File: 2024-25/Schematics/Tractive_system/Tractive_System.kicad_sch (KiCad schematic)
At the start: 20 parts, among them J1 Conn_01x03_Pin, J13 Conn_01x03_Pin, J14 BU-P72930-0, J15 UPCR012ALS2, J16 UPCR012ALS1, J17 EM30MSD-A(06), J18 1-66103-8, J19 1-66399-0, J3 Molex 33472-4001, J4 UPCR012ALS2, J5 Conn_01x02_Pin, J6 UPCR012ALS1, J7 Conn_01x02_Socket

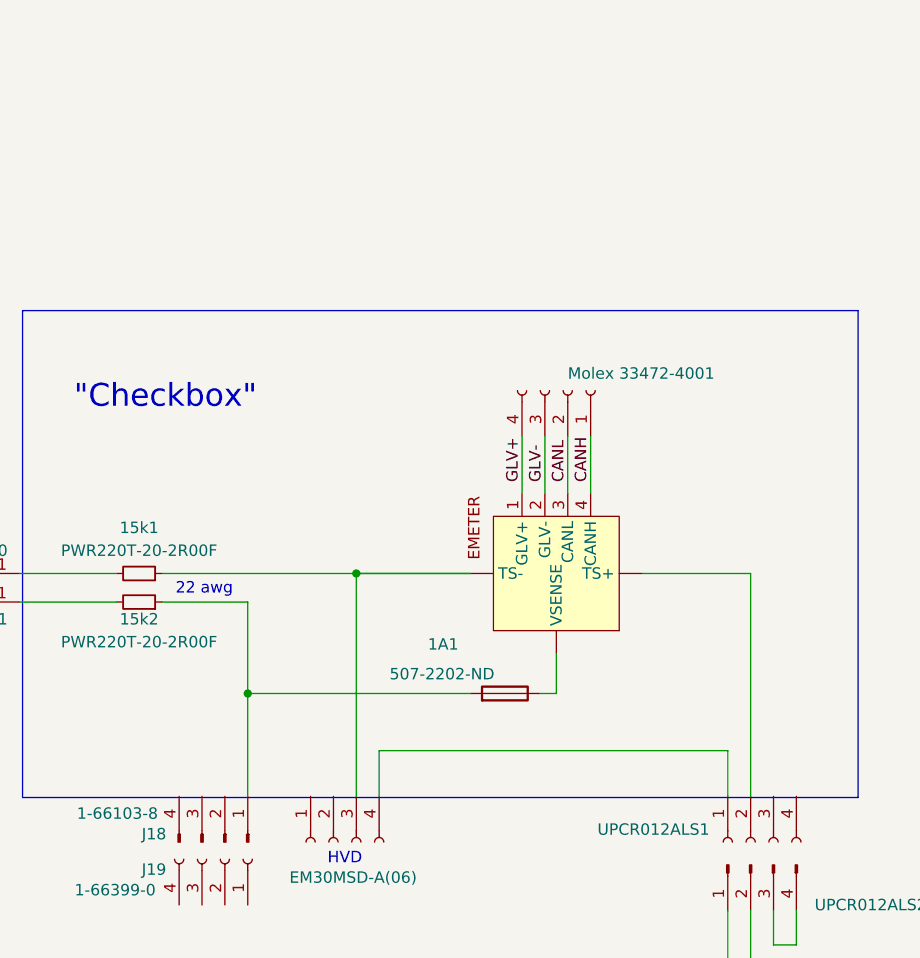
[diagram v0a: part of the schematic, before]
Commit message: Updated tractive system schematic to new energy meter
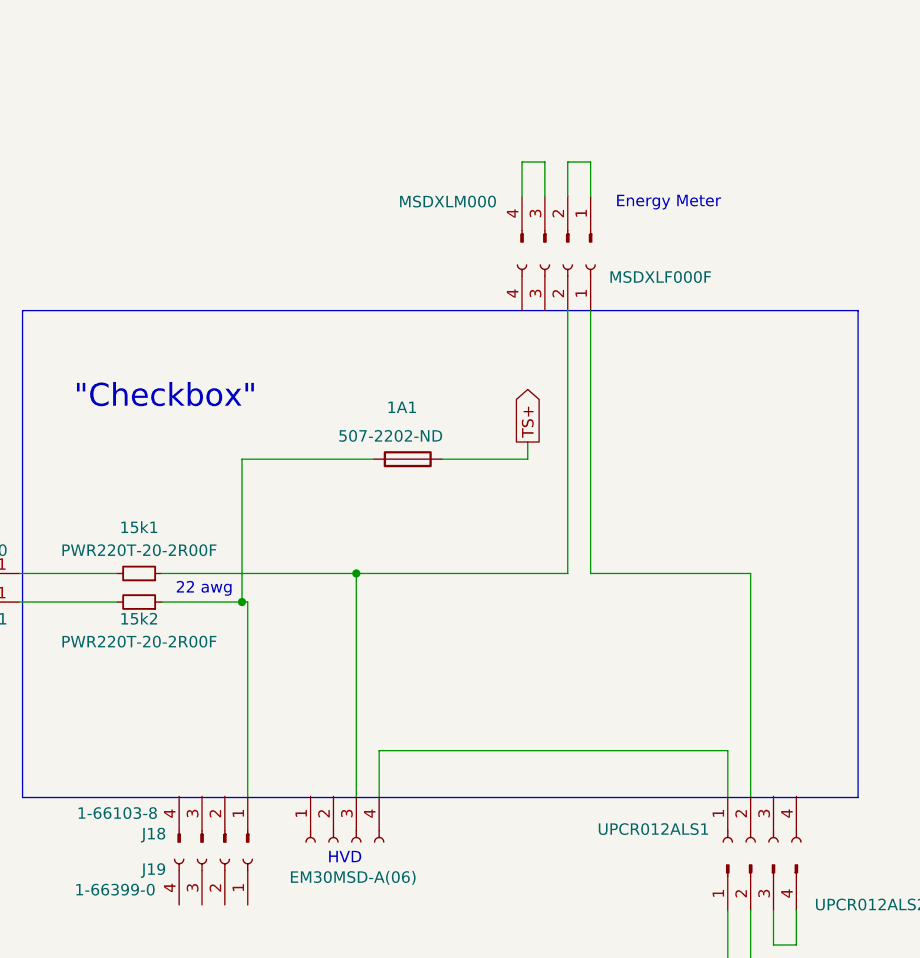
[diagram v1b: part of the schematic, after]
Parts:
- removed J3: Molex 33472-4001, symbol Connector:Conn_01x04_Socket
- removed U1: ~, symbol FSAE:Emeter
- added J8: MSDXLF000F, symbol Connector:Conn_01x04_Socket
- added J9: MSDXLM000, symbol Connector:Conn_01x04_Pin
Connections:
- net at 15k1.1, J17.3 (Pin_3): now also J8.2 (Pin_2)
- net at J16.2 (Pin_2): now also J8.1 (Pin_1)
- net TS+: now reaches 1A1.1
- new net: J9.1 (Pin_1), J9.2 (Pin_2)
- new net: J9.3 (Pin_3), J9.4 (Pin_4)
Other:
- note added: "Energy Meter"
- moved on the sheet: 1A1

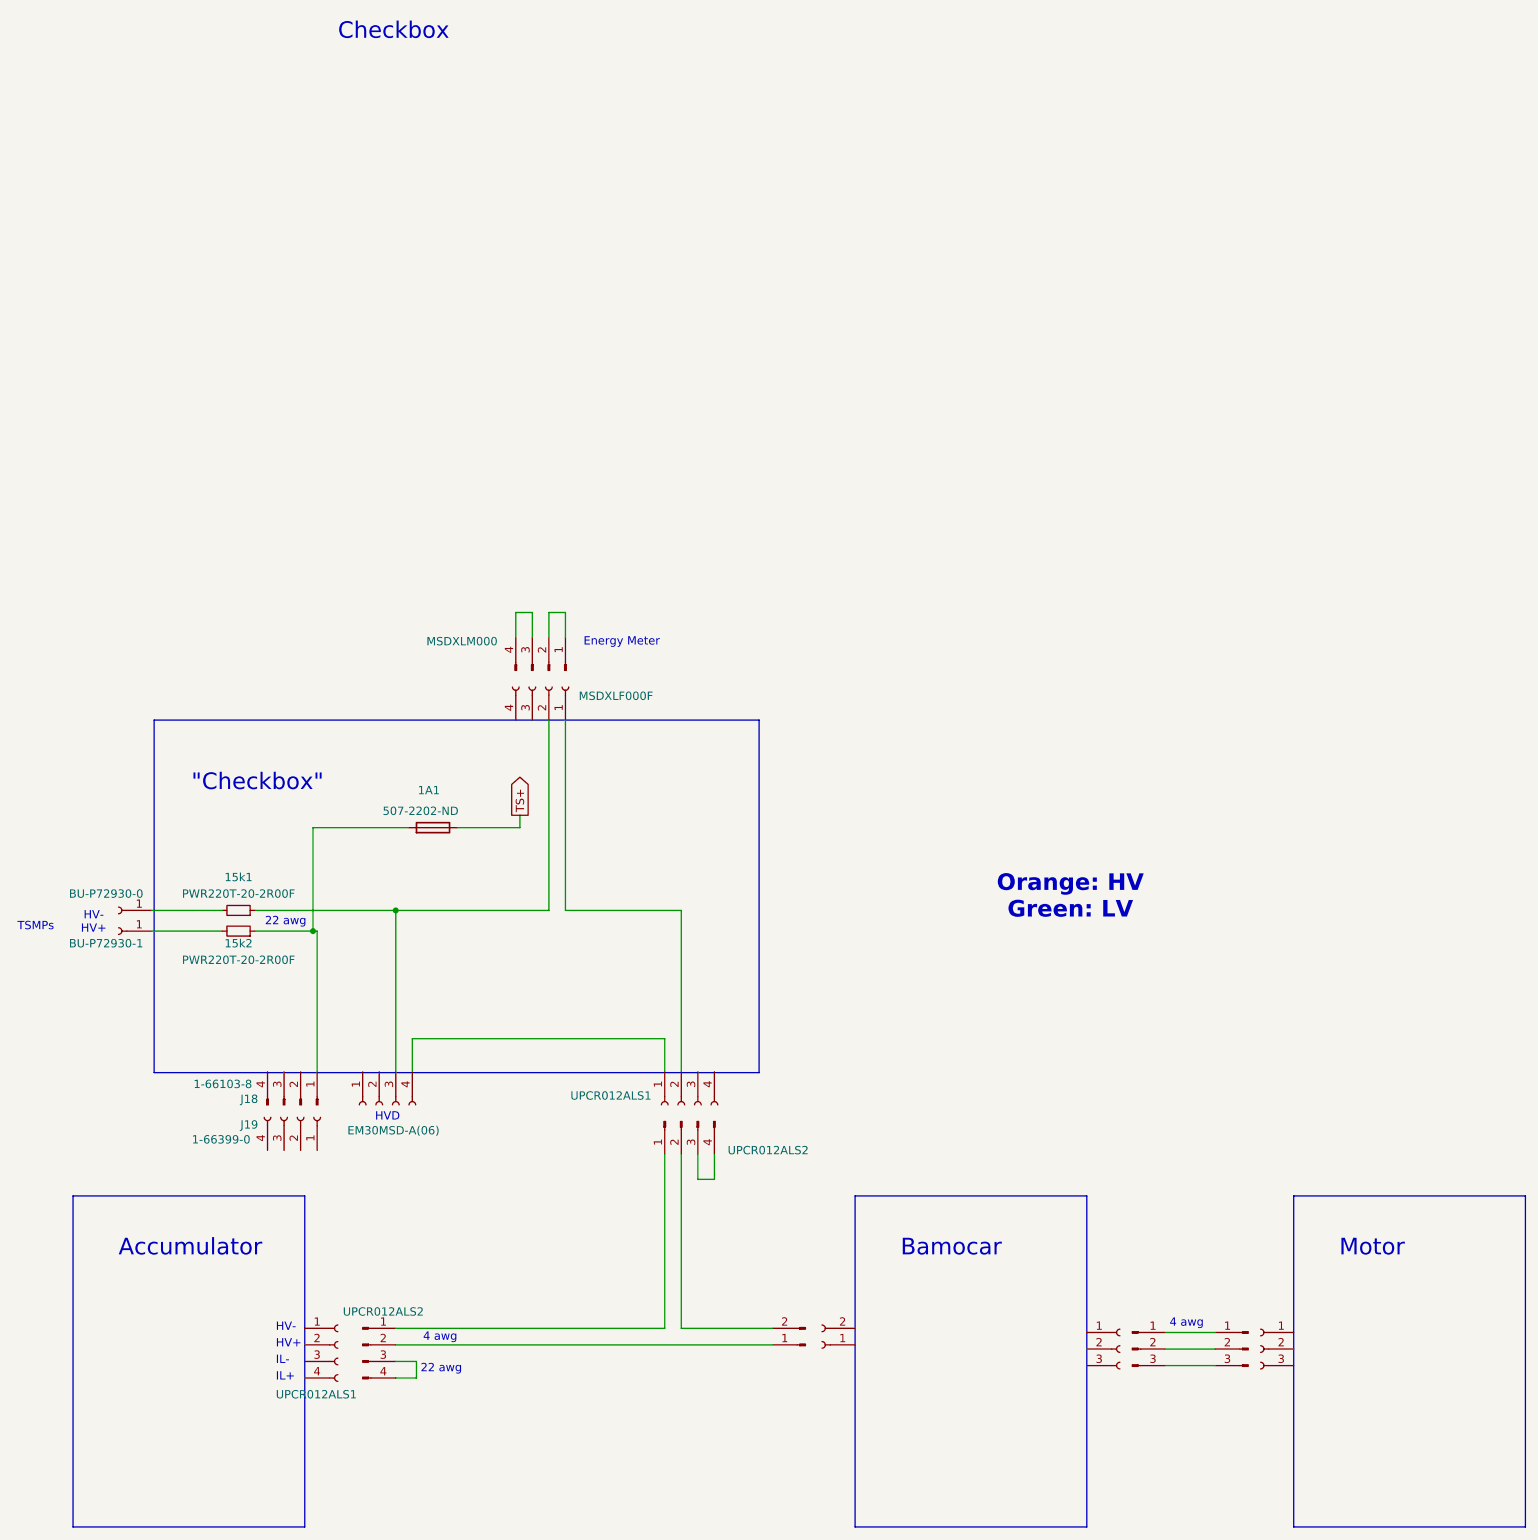
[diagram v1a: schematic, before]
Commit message: fixed some schematics
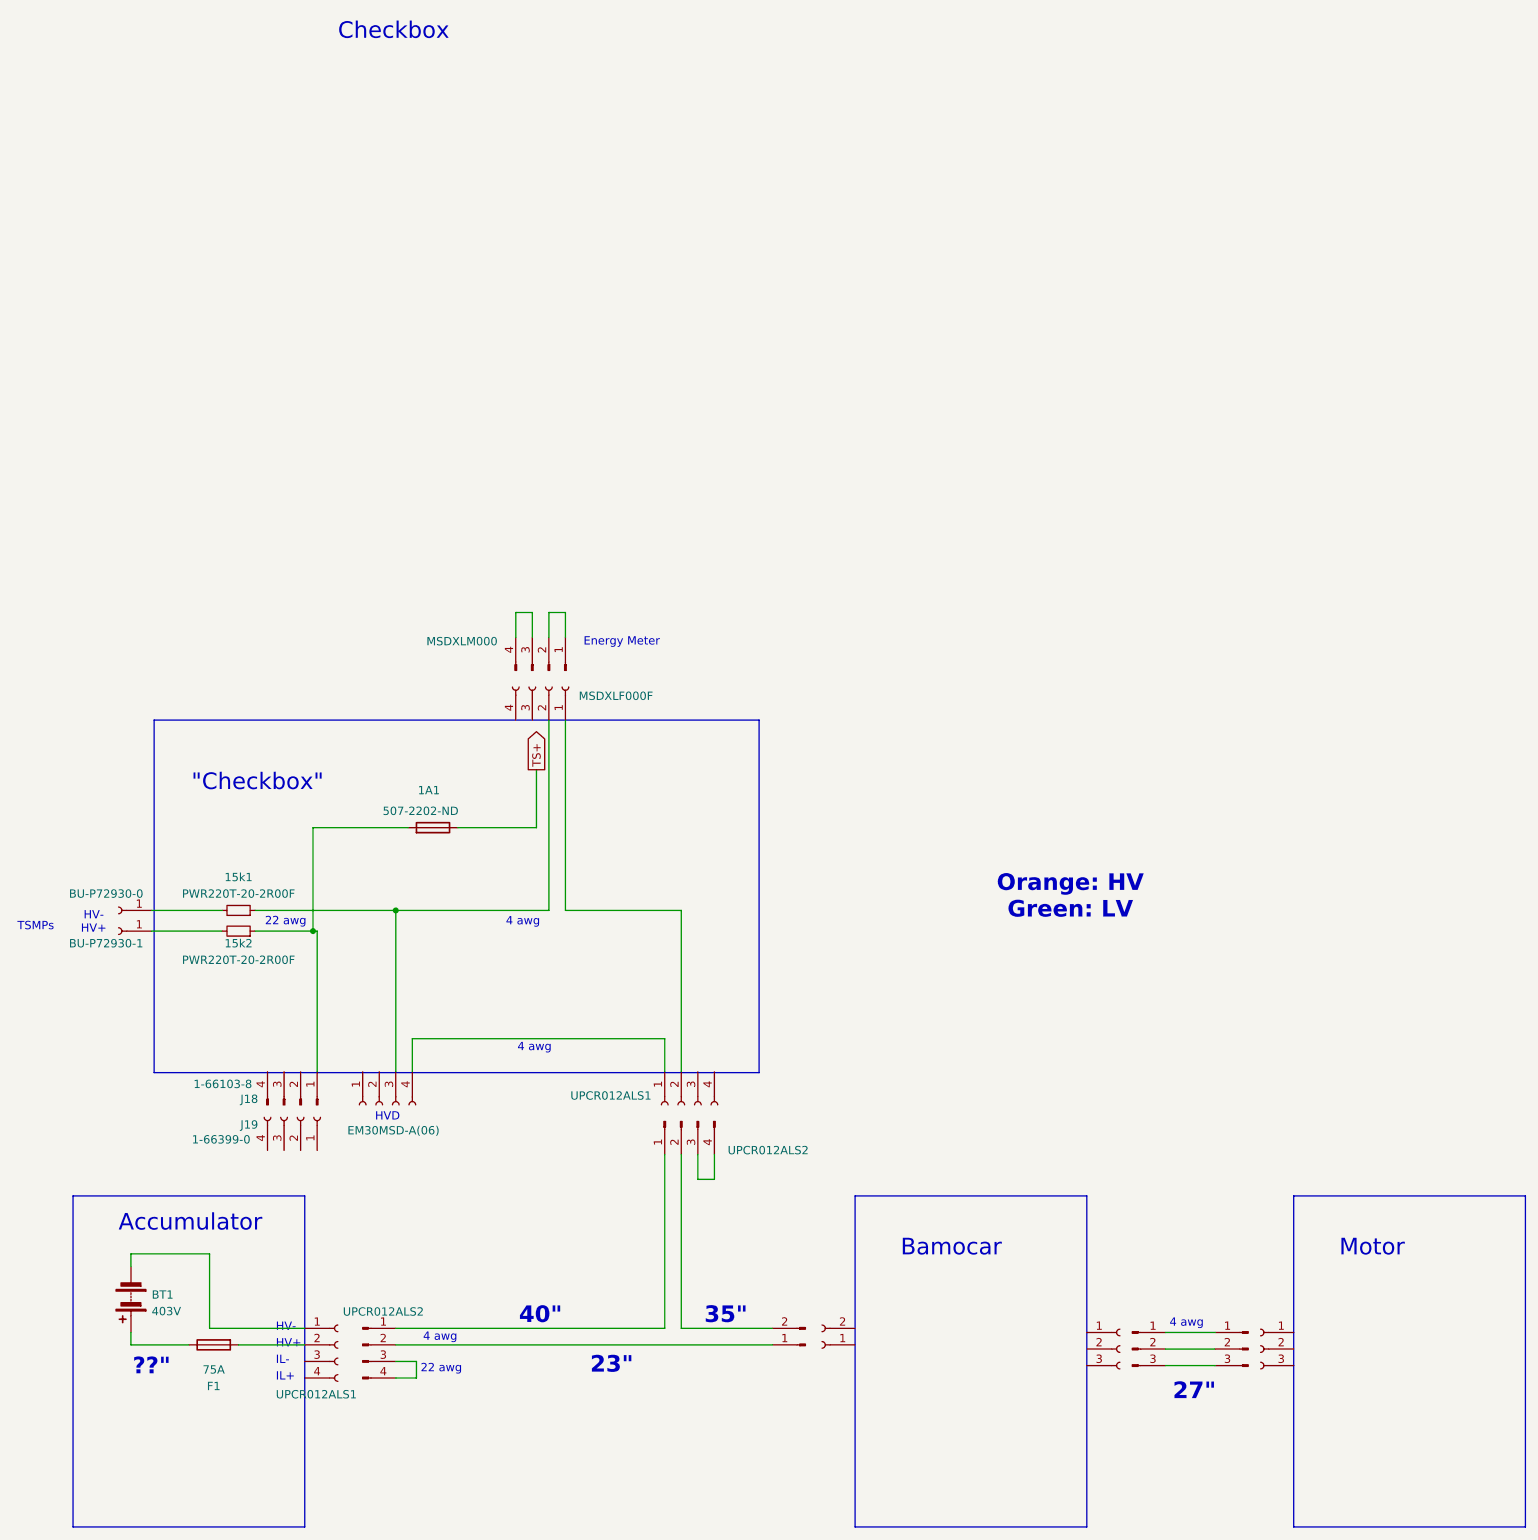
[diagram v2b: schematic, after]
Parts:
- added BT1: 403V, symbol Device:Battery
- added F1: 75A, symbol Device:Fuse
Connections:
- net at J6.1 (Pin_1): now also BT1.2 (-)
- net at J6.2 (Pin_2): now also F1.2
- new net: BT1.1 (+), F1.1
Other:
- note added: "23""
- note added: "27""
- note added: "35""
- note added: "40""
- note added: "??""

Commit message: ESF fixes
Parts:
- renumbered 1A1 to 1A
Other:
- note added: "Orange: HV Green: LV Thick wire: 4 awg thin wire: 22 awg"
- note added: "connected via ring terminals"
- note removed: "??""
- note removed: "Orange: HV Green: LV"
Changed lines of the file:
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@@
 		)
 	)
-	(text "Orange: HV\nGreen: LV"
-		(exclude_from_sim no)
-		(at 251.46 126.238 0)
+	(text "Orange: HV\nGreen: LV\n\nThick wire: 4 awg\nthin wire: 22 awg"
+		(exclude_from_sim no)
+		(at 252.222 133.35 0)
 		(effects
 			(font
@@
 			(font
 				(size 1.27 1.27)
+			)
+		)
+	)
+	(text "connected via \nring terminals"
+		(exclude_from_sim no)
+		(at 269.748 185.166 0)
+		(effects
+			(font
+				(size 1.905 1.905)
 			)
 		)
@@
 		)
 	)
-	(text "??\""
-		(exclude_from_sim no)
-		(at 110.49 198.374 0)
+	(text "4 awg"
+		(exclude_from_sim no)
+		(at 166.624 150.114 0)
+		(effects
+			(font
+				(size 1.27 1.27)
+			)
+			(justify left bottom)
+		)
+	)
+	(text "35\""
+		(exclude_from_sim no)
+		(at 198.628 190.5 0)
 		(effects
 			(font
@@
 		)
 	)
-	(text "4 awg"
-		(exclude_from_sim no)
-		(at 166.624 150.114 0)
-		(effects
-			(font
-				(size 1.27 1.27)
-			)
-			(justify left bottom)
-		)
-	)
-	(text "35\""
-		(exclude_from_sim no)
-		(at 198.628 190.5 0)
-		(effects
-			(font
-				(size 2.54 2.54)
-				(thickness 0.508)
-				(bold yes)
-				(color 0 132 132 1)
-			)
-		)
-	)
 	(text "IL-\n"
 		(exclude_from_sim no)
@@
 			)
 			(justify left bottom)
+		)
+	)
+	(text "connected via \nring terminals"
+		(exclude_from_sim no)
+		(at 215.392 201.93 0)
+		(effects
+			(font
+				(size 1.905 1.905)
+			)
 		)
 	)
@@
 		(on_board yes)
 		(dnp no)
-		(property "Reference" "1A1"
+		(property "Reference" "1A"
 			(at 153.035 109.855 90)
 			(effects
@@
 			(project "Tractive_System"
 				(path "/005a60e9-6b1d-4b23-9e8f-781ba2182e66"
-					(reference "1A1")
-					(unit 1)
-				)
+					(reference "1A")
+					(unit 1)
+				)

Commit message: integration cleanups
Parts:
- removed 1A: 507-2202-ND, symbol Device:Fuse
- removed J8: MSDXLF000F, symbol Connector:Conn_01x04_Socket
- removed J9: MSDXLM000, symbol Connector:Conn_01x04_Pin
- added 1A1: Fuse, symbol Device:Fuse
- added J10: 206429-1, symbol Connector:Conn_01x04_Socket
- added J3: 211102-1, symbol Connector:Conn_01x04_Pin
- added J8: MSDXLF000F, symbol Connector:Conn_01x10_Socket
- added J9: MSDXLM000, symbol Connector:Conn_01x10_Pin
- J18: value 1-66103-8 -> 211102-1
- J19: value 1-66399-0 -> 206429-1
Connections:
- net at J16.2 (Pin_2): now also J8.1 (Pin_1)
- net at 15k1.1, J17.3 (Pin_3): now also J8.2 (Pin_2)
- net at J15.2 (Pin_2), J5.2 (Pin_2): now also J19.3 (Pin_3)
- net at BT1.2 (-), J6.1 (Pin_1): now also 15k2.2, 1A1.1
- net at 15k2.1: now also J3.1 (Pin_1); no longer J18.1 (Pin_1)
- net at BU-P72930-1.1 (Pin_1): now also J18.1 (Pin_1); no longer 15k2.2
- net at J19.1 (Pin_1): now also J10.1 (Pin_1)
- net at J19.2 (Pin_2): now also J10.2 (Pin_2)
- net HV+_sense: now reaches J18.2 (Pin_2)
- net HV+_sense: now also J8.3 (Pin_3)
- net to discharge: now reaches J18.3 (Pin_3)
- new net: 1A1.2, J3.2 (Pin_2)
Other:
- moved on the sheet: 15k1, BT1, BU-P72930-1, F1
